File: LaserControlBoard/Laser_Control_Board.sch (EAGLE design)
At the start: 22 parts, among them J1 Servo Header, J2 FTDI Header, U1 ATMEGA328P_TQFP, Y1 16MHz

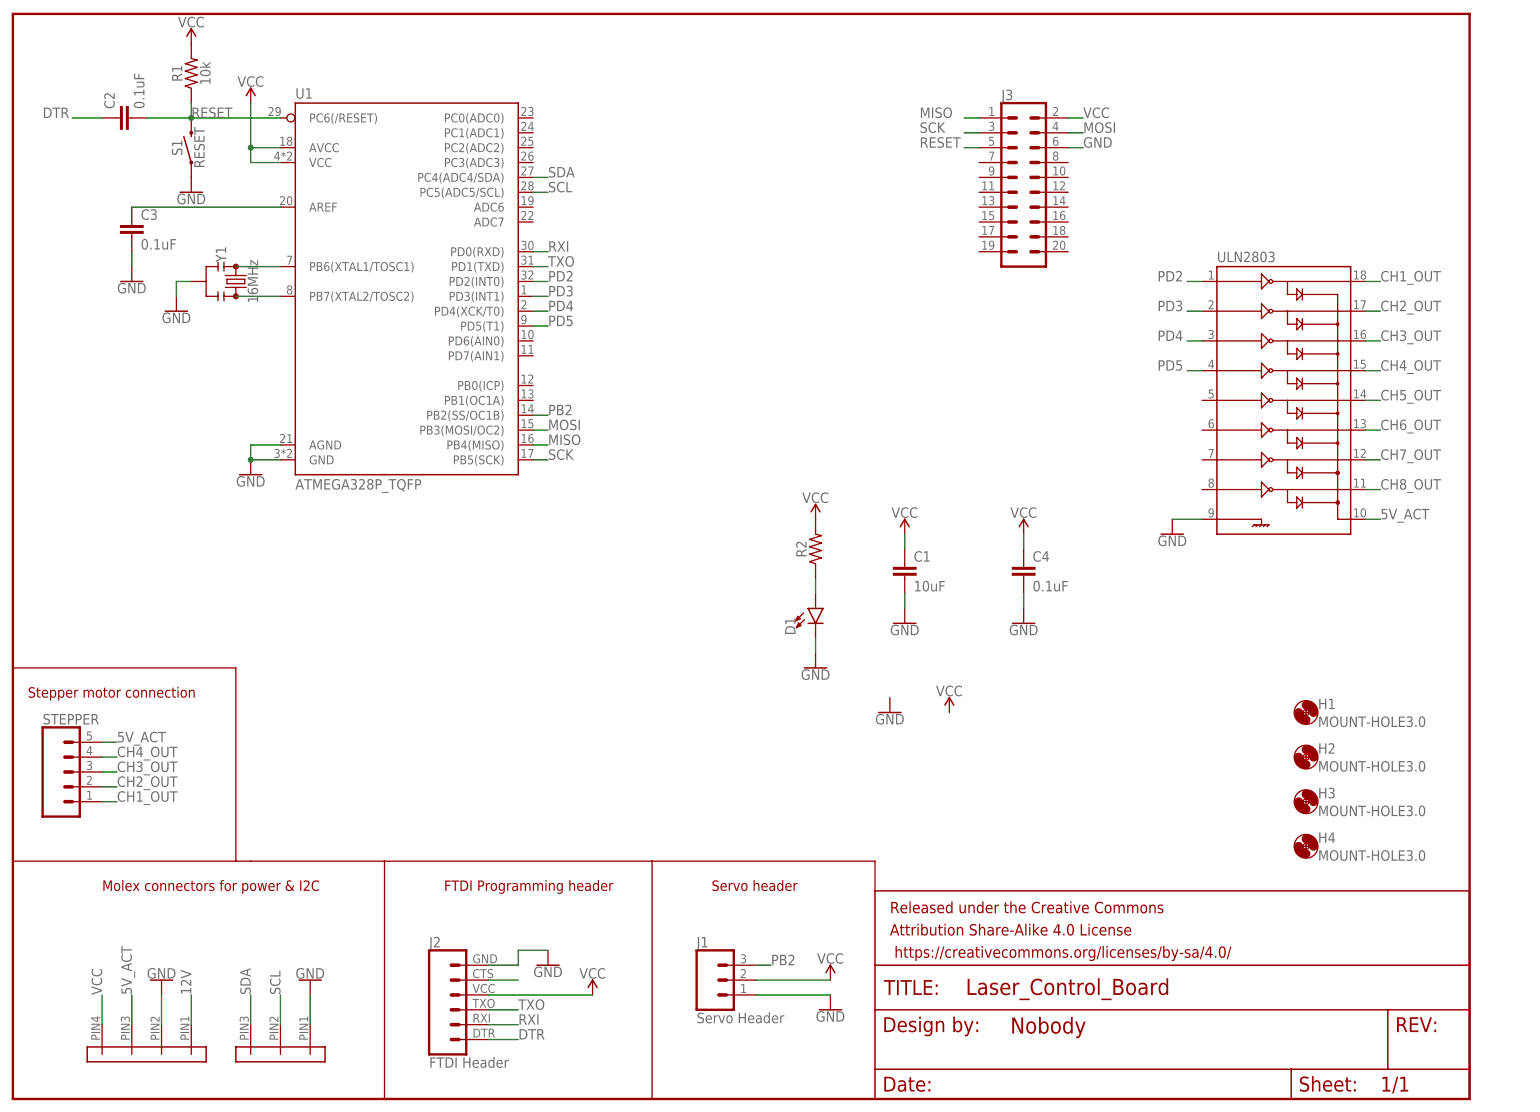
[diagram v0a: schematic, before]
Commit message: Added Mosfet to library. First rev of subsystem control board finished and routed.
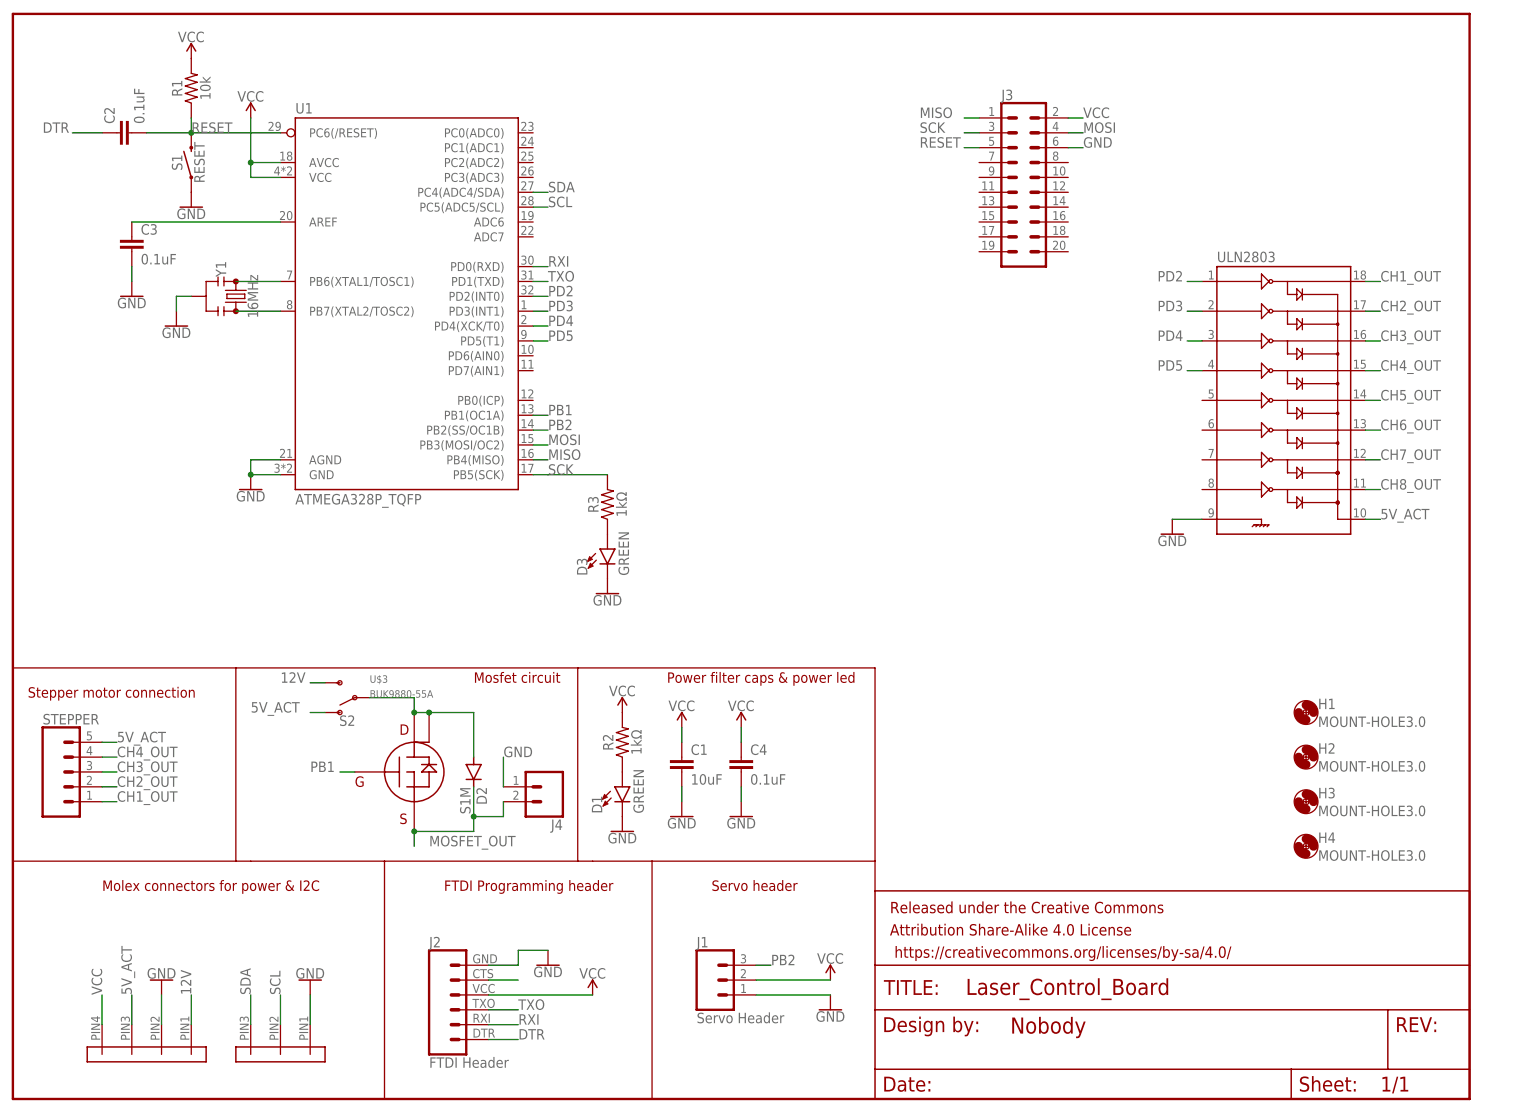
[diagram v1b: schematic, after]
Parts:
- added D2: S1M, diode:S1M
- added D3: GREEN, SparkFun-LED:LED-GREEN1206
- added J4: (no value), SparkFun-Connectors:CONN_02
- added R3: 1kΩ, SparkFun-Resistors:RESISTOR0805
- added S2: (no value), SparkFun-Switches:SWITCH-SPDT-PTH-11.6X4.0MM
- added U$3: BUK9880-55A, PowerManagementParts:BUK9880-55A
- D1: value (none) -> GREEN; device SparkFun-LED:LED1206 -> SparkFun-LED:LED-GREEN1206
- R2: value (none) -> 1kΩ
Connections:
- new net MOSFET_OUT: D2.C, J4.2, U$3.SOURCE
- new net N$1: D2.A, S2.P, U$3.DRAIN, U$3.DRAIN_TAB
- new net N$7: D3.A, R3.1
- new net PB1: U$3.GATE, U1.PB1(OC1A)
- net 12V: now also S2.S
- net 5V_ACT: now also S2.O
- net GND: now also D3.C, J4.1
- net SCK: now also R3.2
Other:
- note added: "Mosfet circuit"
- note added: "Power filter caps & power led"
- moved on the sheet: C1, C2, C3, C4, R1, R2, S1, U1, Y1

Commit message: Redid MOSFET symbol. MOSFET is now Nchan on Low-side.
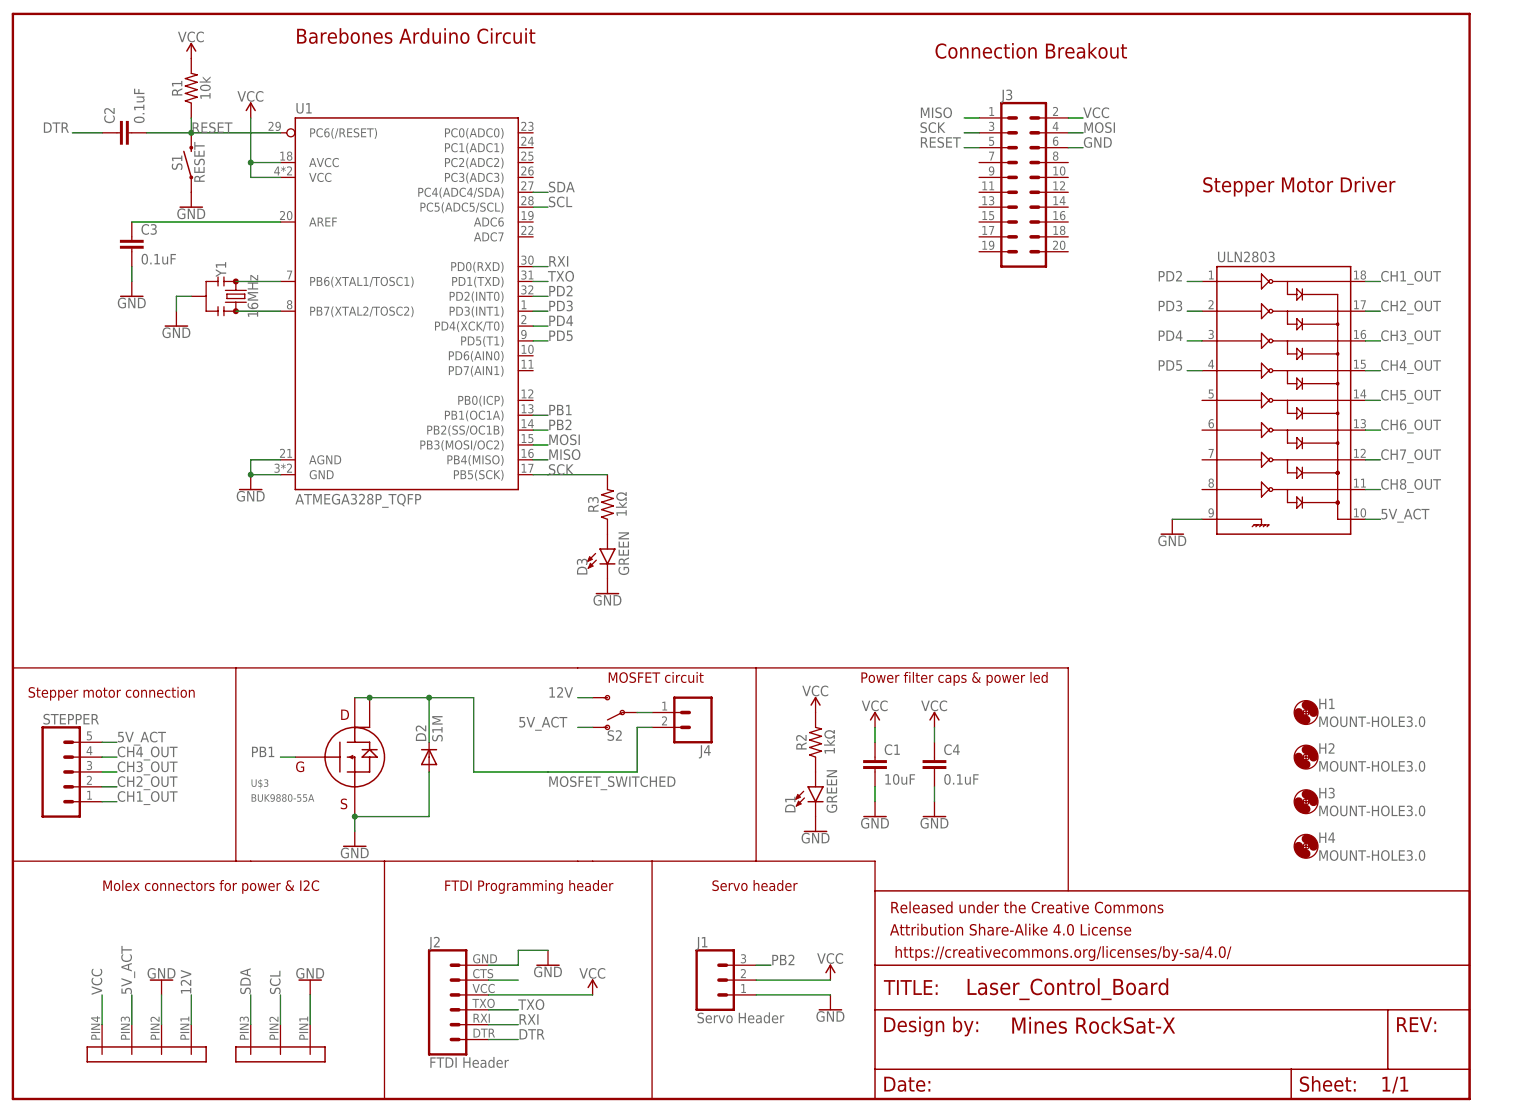
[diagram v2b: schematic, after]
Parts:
- FRAME1: DESIGNER (none) -> Mines RockSat-X; VERSION (none) -> 1
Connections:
- removed net MOSFET_OUT: D2.C, J4.2, U$3.SOURCE
- new net MOSFET_SWITCHED: D2.C, J4.2, U$3.DRAIN, U$3.DRAIN_TAB
- net GND: now also D2.A, U$3.SOURCE; no longer J4.1
- net N$1: now also J4.1; no longer D2.A, U$3.DRAIN, U$3.DRAIN_TAB
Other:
- note added: "Barebones Arduino Circuit"
- note added: "Connection Breakout"
- note added: "MOSFET circuit"
- note added: "Stepper Motor Driver"
- note removed: "Mosfet circuit"
- moved on the sheet: C1, C4, D1, J4, R2, S2

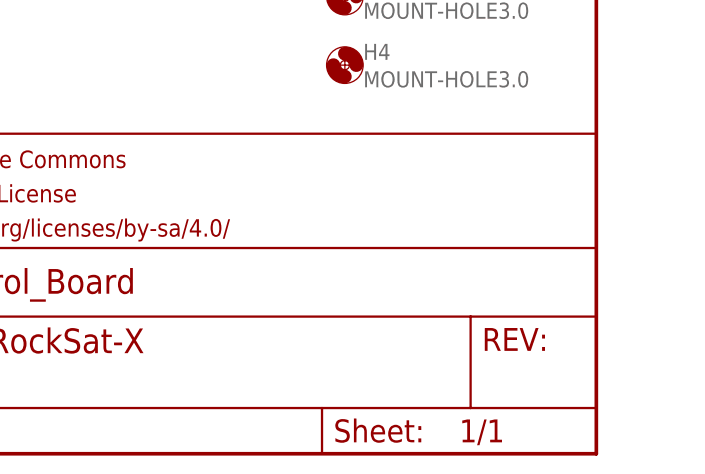
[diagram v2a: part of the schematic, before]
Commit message: Added AKA to nameplate
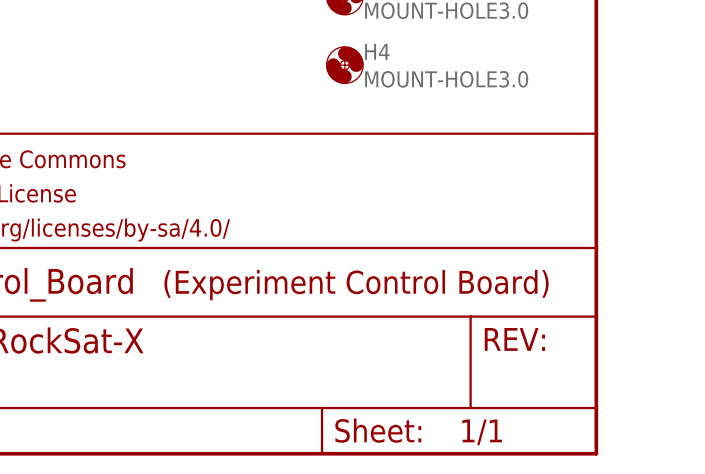
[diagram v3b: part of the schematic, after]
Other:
- note added: "(Experiment Control Board)"
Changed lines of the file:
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@@
 <text x="203.2" y="154.94" size="2.54" layer="94">Stepper Motor Driver</text>
 <text x="157.48" y="177.8" size="2.54" layer="94">Connection Breakout</text>
+<text x="200.66" y="17.78" size="2.54" layer="94" font="vector">(Experiment Control Board)</text>
 </plain>
 <instances>

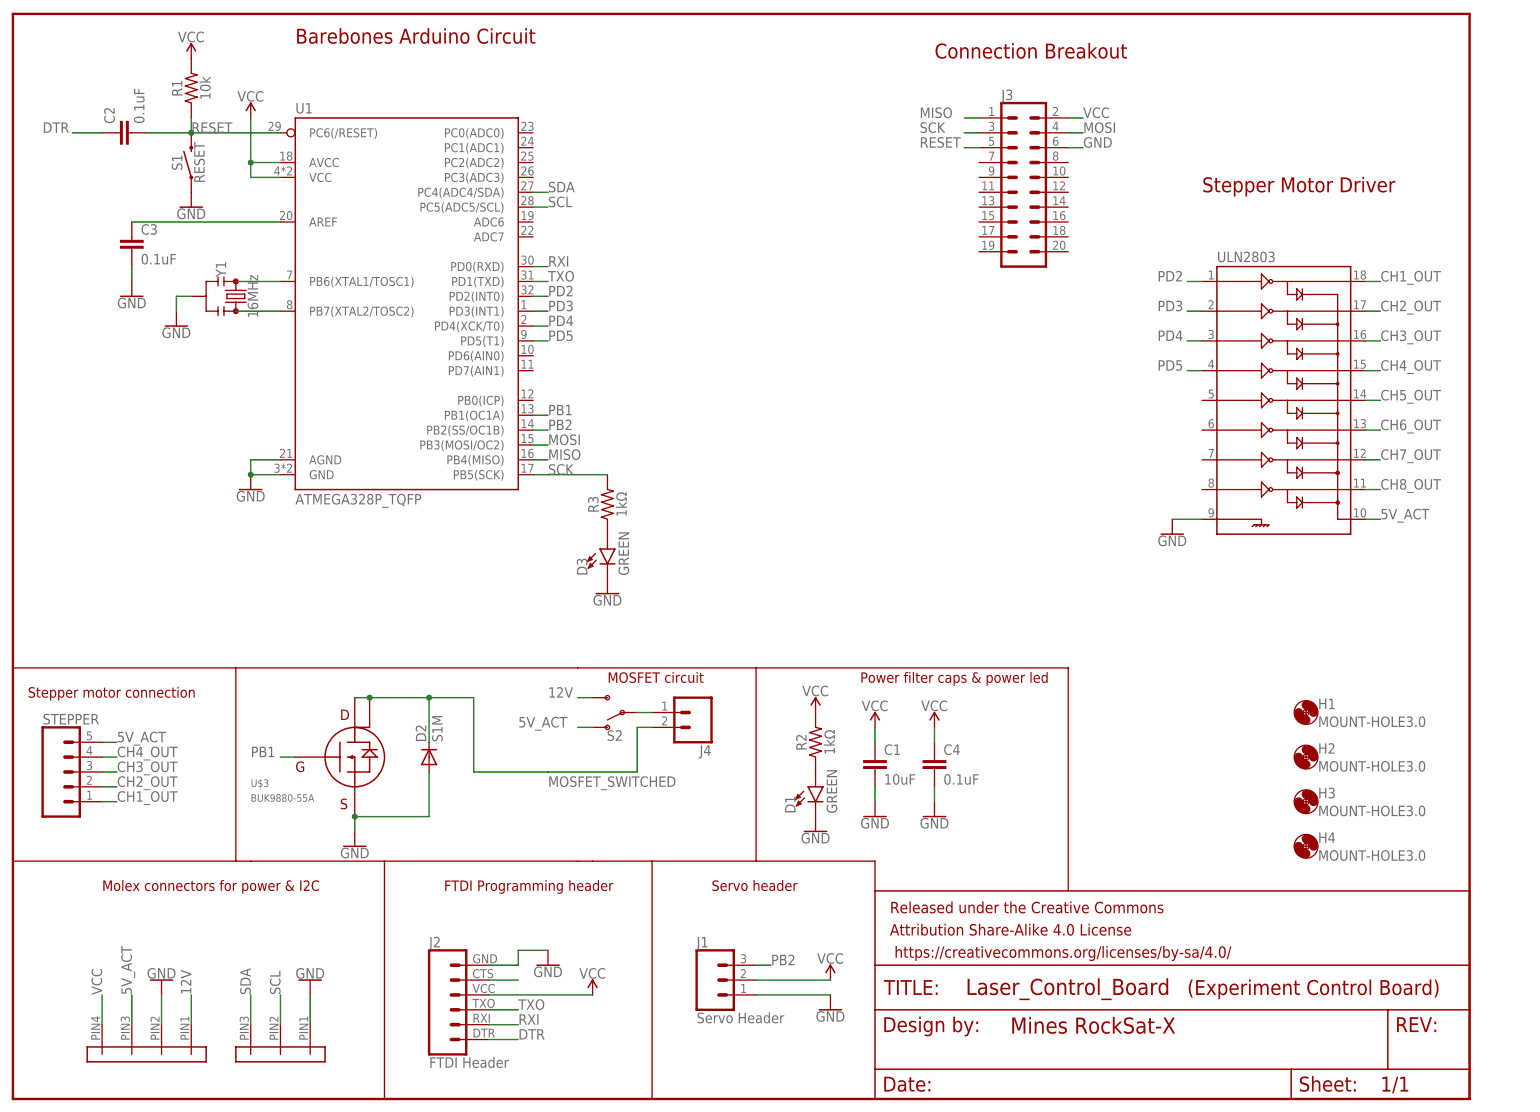
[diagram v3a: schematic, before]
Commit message: Added second MOSFET to subsystem control board and rerouted.
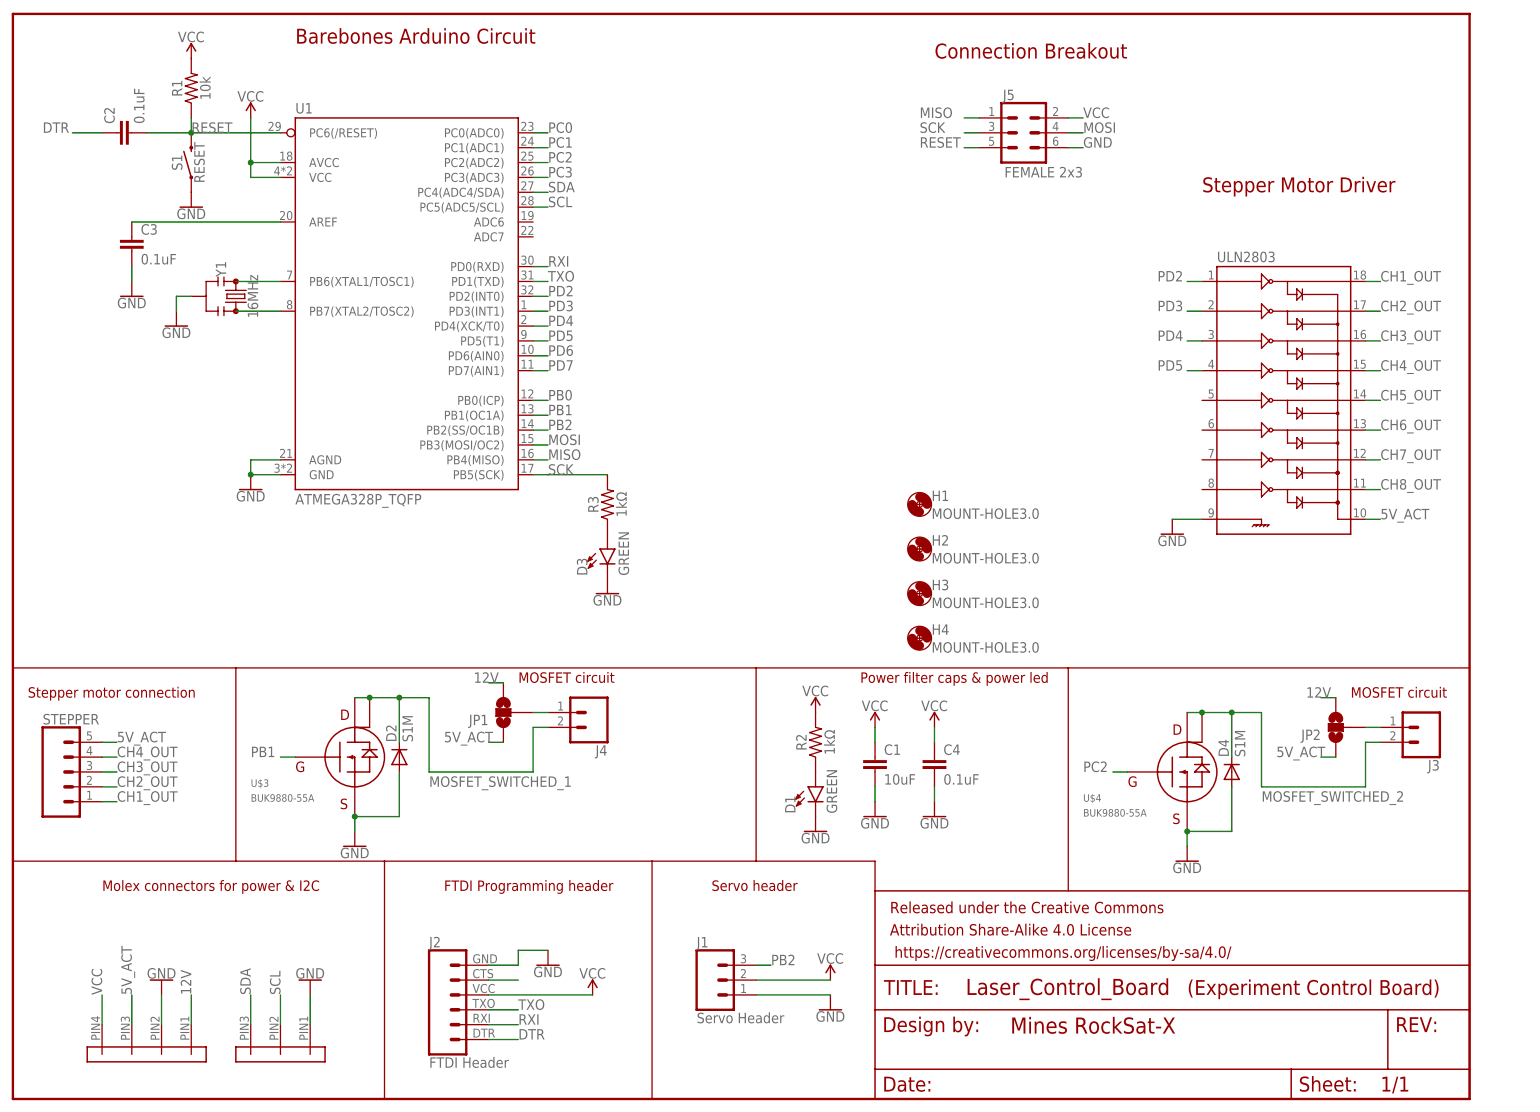
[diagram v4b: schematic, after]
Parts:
- removed S2: (no value), SparkFun-Switches:SWITCH-SPDT-PTH-11.6X4.0MM
- added D4: S1M, diode:S1M
- added J5: FEMALE 2x3, SparkFun-Connectors:CONN_03X2FEMALE
- added JP1, JP2: JUMPER-SMT_3_NO_NO_SILK, SparkFun-Jumpers:JUMPER-SMT_3_NO_NO_SILK
- added U$4: BUK9880-55A, PowerManagementParts:BUK9880-55A
- J3: device SparkFun-Connectors:CONN_10X2 -> SparkFun-Connectors:CONN_02
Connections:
- net MOSFET_SWITCHED renamed MOSFET_SWITCHED_1
- new net MOSFET_SWITCHED_2: D4.C, J3.2, U$4.DRAIN, U$4.DRAIN_TAB
- new net N$8: J3.1, JP2.2
- new net PB0: U1.PB0(ICP)
- new net PC0: U1.PC0(ADC0)
- new net PC1: U1.PC1(ADC1)
- new net PC2: U$4.GATE, U1.PC2(ADC2)
- new net PC3: U1.PC3(ADC3)
- new net PD6: U1.PD6(AIN0)
- new net PD7: U1.PD7(AIN1)
- net 12V: now also JP1.3, JP2.3; no longer S2.S
- net 5V_ACT: now also JP1.1, JP2.1; no longer S2.O
- net GND: now also D4.A, J5.6, U$4.SOURCE; no longer J3.6
- net MISO: now also J5.1; no longer J3.1
- net MOSI: now also J5.4; no longer J3.4
- net N$1: now also JP1.2; no longer S2.P
- net RESET: now also J5.5; no longer J3.5
- net SCK: now also J5.3; no longer J3.3
- net VCC: now also J5.2; no longer J3.2
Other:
- moved on the sheet: D2, H1, H2, H3, H4, J4
